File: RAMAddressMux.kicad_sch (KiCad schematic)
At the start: 18 parts, among them J1 74LS257

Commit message: update traces
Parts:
- removed RA2, RA3: 1K, Resistor_THT:R_Array_SIP8, symbol Device:R_Network07_US
- added RA02, RA03: 1K, Resistor_THT:R_Array_SIP8, symbol Device:R_Network07_US
- A2, C11, C14, D1, D2, E1, F1, H1: footprint Apple:DIP-14_W7.62mm -> Package_DIP:DIP-14_W7.62mm
- C12, E11, E12, E13, E14, E2, F2, J1: footprint Apple:DIP-16_W7.62mm -> Package_DIP:DIP-16_W7.62mm
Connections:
- net +5V: now also RA02.1 (common)
- net GND: now also RA03.1 (common)
- net RA0: now also RA02.7 (R6), RA03.7 (R6)
- net RA1: now also RA02.5 (R4), RA03.5 (R4)
- net RA2: now also RA02.3 (R2), RA03.3 (R2)
- net RA3: now also RA02.8 (R7), RA03.8 (R7)
- net RA4: now also RA02.6 (R5), RA03.6 (R5)
- net RA5: now also RA02.4 (R3), RA03.4 (R3)
- no-connect marks 4 -> 9

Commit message: more tracing
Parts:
- added unit 5 of H1
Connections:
- net +5V: now also H1.14 (VCC)
- net GND: now also H1.7 (GND)

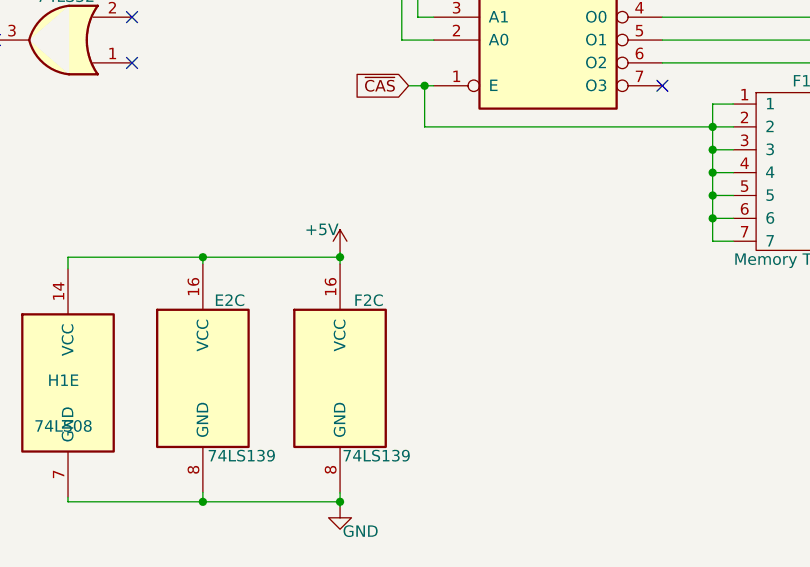
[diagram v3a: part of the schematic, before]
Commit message: more tracing - down to row E
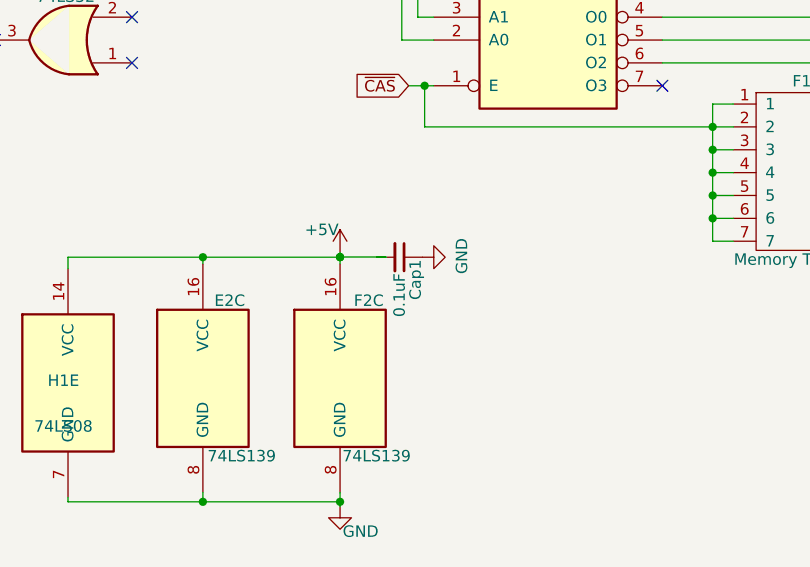
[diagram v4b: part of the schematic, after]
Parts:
- added Cap1: 0.1uF, Capacitor_THT:C_Disc_D5.0mm_W2.5mm_P5.00mm, symbol Device:C_Small
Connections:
- net +5V: now also Cap1.2
- net GND: now also Cap1.1
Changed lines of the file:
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@@
   (junction (at 86.868 108.966) (diameter 0) (color 0 0 0 0)
+  )
+  (junction (at 228.346 196.829) (diameter 0) (color 0 0 0 0)
   )
   (junction (at 113.538 91.186) (diameter 0) (color 0 0 0 0)
@@
     (stroke (width 0) (type default))
   )
+  (wire (pts (xy 228.346 196.829) (xy 228.346 196.85))
+    (stroke (width 0) (type default))
+  )
   (wire (pts (xy 85.598 86.106) (xy 87.376 86.106))
     (stroke (width 0) (type default))
@@
     (stroke (width 0) (type default))
   )
+  (wire (pts (xy 233.426 196.829) (xy 233.426 196.85))
+    (stroke (width 0) (type default))
+  )
   (wire (pts (xy 213.36 127) (xy 224.282 127))
     (stroke (width 0) (type default))
@@
     (stroke (width 0) (type default))
   )
+  (wire (pts (xy 228.346 196.829) (xy 233.426 196.829))
+    (stroke (width 0) (type default))
+  )
   (wire (pts (xy 180.34 119.38) (xy 187.96 119.38))
     (stroke (width 0) (type default))
@@
     (stroke (width 0) (type default))
   )
-  (wire (pts (xy 228.346 196.342) (xy 228.346 196.85))
+  (wire (pts (xy 228.346 196.342) (xy 228.346 196.829))
     (stroke (width 0) (type default))
   )
@@
   )
   (wire (pts (xy 235.204 172.72) (xy 238.76 172.72))
+    (stroke (width 0) (type default))
+  )
+  (wire (pts (xy 233.426 196.85) (xy 232.41 196.85))
     (stroke (width 0) (type default))
   )
@@
     )
   )
+  (symbol (lib_id "Device:C_Small") (at 234.95 196.85 270) (unit 1)
+    (in_bom yes) (on_board yes) (dnp no)
+    (property "Reference" "Cap1" (at 236.728 197.104 0)
+      (effects (font (size 1.27 1.27)) (justify left))
+    )
+    (property "Value" "0.1uF" (at 234.95 198.628 0)
+      (effects (font (size 1.27 1.27)) (justify left))
+    )
+    (property "Footprint" "Capacitor_THT:C_Disc_D5.0mm_W2.5mm_P5.00mm" (at 234.95 196.85 0)
+      (effects (font (size 1.27 1.27)) hide)
+    )
+    (property "Datasheet" "~" (at 234.95 196.85 0)
+      (effects (font (size 1.27 1.27)) hide)
+    )
+    (pin "1")
+    (pin "2")
+    (instances
+      (project "AppleII"
+        (path "/f1f08369-4db3-46f7-9b89-a5d3cfbed55a/00000000-0000-0000-0000-00006016cde0"
+          (reference "Cap1") (unit 1)
+        )
+        (path "/f1f08369-4db3-46f7-9b89-a5d3cfbed55a/00000000-0000-0000-0000-00006039aab4"
+          (reference "Cap3") (unit 1)
+        )
+        (path "/f1f08369-4db3-46f7-9b89-a5d3cfbed55a/00000000-0000-0000-0000-000060210f9e"
+          (reference "Cap17") (unit 1)
+        )
+      )
+    )
+  )
   (symbol (lib_id "74xx:74LS08") (at 198.12 210.82 0) (unit 5)
     (in_bom yes) (on_board yes) (dnp no)
@@
         )
       )
+    )
+  )
+  (symbol (lib_id "power:GND") (at 237.49 196.85 90) (unit 1)
+    (in_bom yes) (on_board yes) (dnp no)
+    (property "Reference" "#PWR013" (at 243.84 196.85 0)
+      (effects (font (size 1.27 1.27)) hide)
+    )
+    (property "Value" "GND" (at 241.8842 196.723 0)
+      (effects (font (size 1.27 1.27)))
+    )
+    (property "Footprint" "" (at 237.49 196.85 0)
+      (effects (font (size 1.27 1.27)) hide)
+    )
+    (property "Datasheet" "" (at 237.49 196.85 0)
+      (effects (font (size 1.27 1.27)) hide)
+    )
+    (pin "1")
+    (instances
+      (project "AppleII"
+        (path "/f1f08369-4db3-46f7-9b89-a5d3cfbed55a/00000000-0000-0000-0000-00006039aab4"
+          (reference "#PWR013") (unit 1)
+        )
+        (path "/f1f08369-4db3-46f7-9b89-a5d3cfbed55a/00000000-0000-0000-0000-000060210f9e"
+          (reference "#PWR016") (unit 1)
+        )
+      )

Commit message: more tracing
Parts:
- added unit 3 of D2
- renumbered Cap1 to Cap17
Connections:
- net +5V: now also D2.14 (VCC)
- net GND: now also D2.7 (GND)
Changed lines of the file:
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@@
   (junction (at 83.312 181.356) (diameter 0) (color 0 0 0 0)
   )
+  (junction (at 198.12 196.85) (diameter 0) (color 0 0 0 0)
+  )
   (junction (at 269.748 189.992) (diameter 0) (color 0 0 0 0)
   )
@@
   )
   (junction (at 296.164 99.568) (diameter 0) (color 0 0 0 0)
+  )
+  (junction (at 198.12 224.028) (diameter 0) (color 0 0 0 0)
   )
   (junction (at 269.748 192.532) (diameter 0) (color 0 0 0 0)
@@
     (stroke (width 0) (type default))
   )
+  (wire (pts (xy 183.388 224.028) (xy 198.12 224.028))
+    (stroke (width 0) (type default))
+  )
   (wire (pts (xy 144.78 226.314) (xy 144.78 225.552))
     (stroke (width 0) (type default))
@@
     (stroke (width 0) (type default))
   )
+  (wire (pts (xy 183.388 196.85) (xy 183.388 198.12))
+    (stroke (width 0) (type default))
+  )
   (wire (pts (xy 130.556 192.532) (xy 132.08 192.532))
     (stroke (width 0) (type default))
@@
     (stroke (width 0) (type default))
   )
+  (wire (pts (xy 198.12 196.85) (xy 183.388 196.85))
+    (stroke (width 0) (type default))
+  )
   (wire (pts (xy 295.402 113.03) (xy 295.402 112.776))
     (stroke (width 0) (type default))
@@
   )
   (wire (pts (xy 264.16 157.48) (xy 297.942 157.48))
+    (stroke (width 0) (type default))
+  )
+  (wire (pts (xy 183.388 223.52) (xy 183.388 224.028))
     (stroke (width 0) (type default))
   )
@@
     )
   )
+  (symbol (lib_id "74xx:74LS20") (at 183.388 210.82 0) (unit 3)
+    (in_bom yes) (on_board yes) (dnp no)
+    (property "Reference" "D2" (at 181.356 205.232 0)
+      (effects (font (size 1.27 1.27)))
+    )
+    (property "Value" "74LS20" (at 182.88 216.408 0)
+      (effects (font (size 1.27 1.27)))
+    )
+    (property "Footprint" "Package_DIP:DIP-14_W7.62mm" (at 183.388 210.82 0)
+      (effects (font (size 1.27 1.27)) hide)
+    )
+    (property "Datasheet" "http://www.ti.com/lit/gpn/sn74LS20" (at 183.388 210.82 0)
+      (effects (font (size 1.27 1.27)) hide)
+    )
+    (pin "1")
+    (pin "2")
+    (pin "4")
+    (pin "5")
+    (pin "6")
+    (pin "10")
+    (pin "12")
+    (pin "13")
+    (pin "8")
+    (pin "9")
+    (pin "14")
+    (pin "7")
+    (instances
+      (project "AppleII"
+        (path "/f1f08369-4db3-46f7-9b89-a5d3cfbed55a/00000000-0000-0000-0000-000060210f9e"
+          (reference "D2") (unit 3)
+        )
+      )
+    )
+  )
   (symbol (lib_id "Device:C_Small") (at 234.95 196.85 270) (unit 1)
     (in_bom yes) (on_board yes) (dnp no)
-    (property "Reference" "Cap1" (at 236.728 197.104 0)
+    (property "Reference" "Cap17" (at 236.728 197.104 0)
       (effects (font (size 1.27 1.27)) (justify left))
     )
@@
     (instances
       (project "AppleII"
-        (path "/f1f08369-4db3-46f7-9b89-a5d3cfbed55a/00000000-0000-0000-0000-00006016cde0"
-          (reference "Cap1") (unit 1)
-        )
-        (path "/f1f08369-4db3-46f7-9b89-a5d3cfbed55a/00000000-0000-0000-0000-00006039aab4"
-          (reference "Cap3") (unit 1)
-        )
         (path "/f1f08369-4db3-46f7-9b89-a5d3cfbed55a/00000000-0000-0000-0000-000060210f9e"
           (reference "Cap17") (unit 1)
@@
   (symbol (lib_id "power:GND") (at 237.49 196.85 90) (unit 1)
     (in_bom yes) (on_board yes) (dnp no)
-    (property "Reference" "#PWR013" (at 243.84 196.85 0)
+    (property "Reference" "#PWR016" (at 243.84 196.85 0)
       (effects (font (size 1.27 1.27)) hide)
     )
@@
     (instances
       (project "AppleII"
-        (path "/f1f08369-4db3-46f7-9b89-a5d3cfbed55a/00000000-0000-0000-0000-00006039aab4"
-          (reference "#PWR013") (unit 1)
-        )
         (path "/f1f08369-4db3-46f7-9b89-a5d3cfbed55a/00000000-0000-0000-0000-000060210f9e"
           (reference "#PWR016") (unit 1)

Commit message: finish tracing
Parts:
- added unit 5 of C14
- added Cap41, Cap44: 0.1uF, Capacitor_THT:C_Disc_D5.0mm_W2.5mm_P5.00mm, symbol Device:C_Small
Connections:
- net +5V: now also C14.14 (VCC), Cap41.2, Cap44.2
- net GND: now also C14.7 (GND), Cap41.1, Cap44.1
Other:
- moved on the sheet: Cap17, D2C, E2C, F2C, H1E

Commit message: beautify resistors
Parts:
- Cap17, Cap41, Cap44: footprint Capacitor_THT:C_Disc_D5.0mm_W2.5mm_P5.00mm -> Apple-II:C_Disc_D5.0mm_W2.5mm_P5.00mm
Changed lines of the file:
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@@
       (effects (font (size 1.27 1.27)) (justify left))
     )
-    (property "Footprint" "Capacitor_THT:C_Disc_D5.0mm_W2.5mm_P5.00mm" (at 179.3633 201.168 0)
+    (property "Footprint" "Apple-II:C_Disc_D5.0mm_W2.5mm_P5.00mm" (at 179.3633 201.168 0)
       (effects (font (size 1.27 1.27)) hide)
     )
@@
       (effects (font (size 1.27 1.27)) (justify left))
     )
-    (property "Footprint" "Capacitor_THT:C_Disc_D5.0mm_W2.5mm_P5.00mm" (at 246.634 203.708 0)
+    (property "Footprint" "Apple-II:C_Disc_D5.0mm_W2.5mm_P5.00mm" (at 246.634 203.708 0)
       (effects (font (size 1.27 1.27)) hide)
     )
@@
       (effects (font (size 1.27 1.27)) (justify left))
     )
-    (property "Footprint" "Capacitor_THT:C_Disc_D5.0mm_W2.5mm_P5.00mm" (at 92.71 149.86 0)
+    (property "Footprint" "Apple-II:C_Disc_D5.0mm_W2.5mm_P5.00mm" (at 92.71 149.86 0)
       (effects (font (size 1.27 1.27)) hide)
     )

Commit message: add ibom
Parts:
- added Cap49: 0.1uF, Apple-II:C_Disc_D5.0mm_W2.5mm_P5.00mm, symbol Device:C_Small
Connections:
- net +5V: now also Cap49.2
- net GND: now also Cap49.1
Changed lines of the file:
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@@
   (junction (at 179.3633 203.708) (diameter 0) (color 0 0 0 0)
+  )
+  (junction (at 181.356 70.104) (diameter 0) (color 0 0 0 0)
   )
   (junction (at 236.982 122.936) (diameter 0) (color 0 0 0 0)
@@
   )
   (wire (pts (xy 295.402 123.19) (xy 303.022 123.19))
+    (stroke (width 0) (type default))
+  )
+  (wire (pts (xy 177.8 70.104) (xy 181.356 70.104))
     (stroke (width 0) (type default))
   )
@@
     )
   )
+  (symbol (lib_id "Device:C_Small") (at 175.26 70.104 270) (unit 1)
+    (in_bom yes) (on_board yes) (dnp no)
+    (property "Reference" "Cap49" (at 177.038 70.358 0)
+      (effects (font (size 1.27 1.27)) (justify left))
+    )
+    (property "Value" "0.1uF" (at 175.26 71.882 0)
+      (effects (font (size 1.27 1.27)) (justify left))
+    )
+    (property "Footprint" "Apple-II:C_Disc_D5.0mm_W2.5mm_P5.00mm" (at 175.26 70.104 0)
+      (effects (font (size 1.27 1.27)) hide)
+    )
+    (property "Datasheet" "~" (at 175.26 70.104 0)
+      (effects (font (size 1.27 1.27)) hide)
+    )
+    (pin "1")
+    (pin "2")
+    (instances
+      (project "AppleII"
+        (path "/f1f08369-4db3-46f7-9b89-a5d3cfbed55a/00000000-0000-0000-0000-000060210f9e"
+          (reference "Cap49") (unit 1)
+        )
+      )
+    )
+  )
   (symbol (lib_id "Device:C_Small") (at 179.3633 201.168 0) (unit 1)
     (in_bom yes) (on_board yes) (dnp no)
@@
         )
       )
+    )
+  )
+  (symbol (lib_id "power:+5V") (at 172.72 70.104 90) (unit 1)
+    (in_bom yes) (on_board yes) (dnp no)
+    (property "Reference" "#PWR055" (at 176.53 70.104 0)
+      (effects (font (size 1.27 1.27)) hide)
+    )
+    (property "Value" "+5V" (at 170.18 72.136 0)
+      (effects (font (size 1.27 1.27)))
+    )
+    (property "Footprint" "" (at 172.72 70.104 0)
+      (effects (font (size 1.27 1.27)) hide)
+    )
+    (property "Datasheet" "" (at 172.72 70.104 0)
+      (effects (font (size 1.27 1.27)) hide)
+    )
+    (pin "1")
+    (instances
+      (project "AppleII"
+        (path "/f1f08369-4db3-46f7-9b89-a5d3cfbed55a/00000000-0000-0000-0000-000060210f9e"
+          (reference "#PWR055") (unit 1)
+        )
+      )
